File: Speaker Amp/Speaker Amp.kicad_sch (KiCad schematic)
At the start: 52 parts, among them J1 USB_C_Receptacle_USB2.0_16P, J2 Screw_Terminal_01x02, J3 Screw_Terminal_01x02, J4 Screw_Terminal_01x02, SW1 SW_Push, SW2 SW_Push, SW3 SW_Push, U1 LD1117S33TR_SOT223, U2 PCM2704CDBR, U3 TDA7297, U4 CH221K, Y1 12M

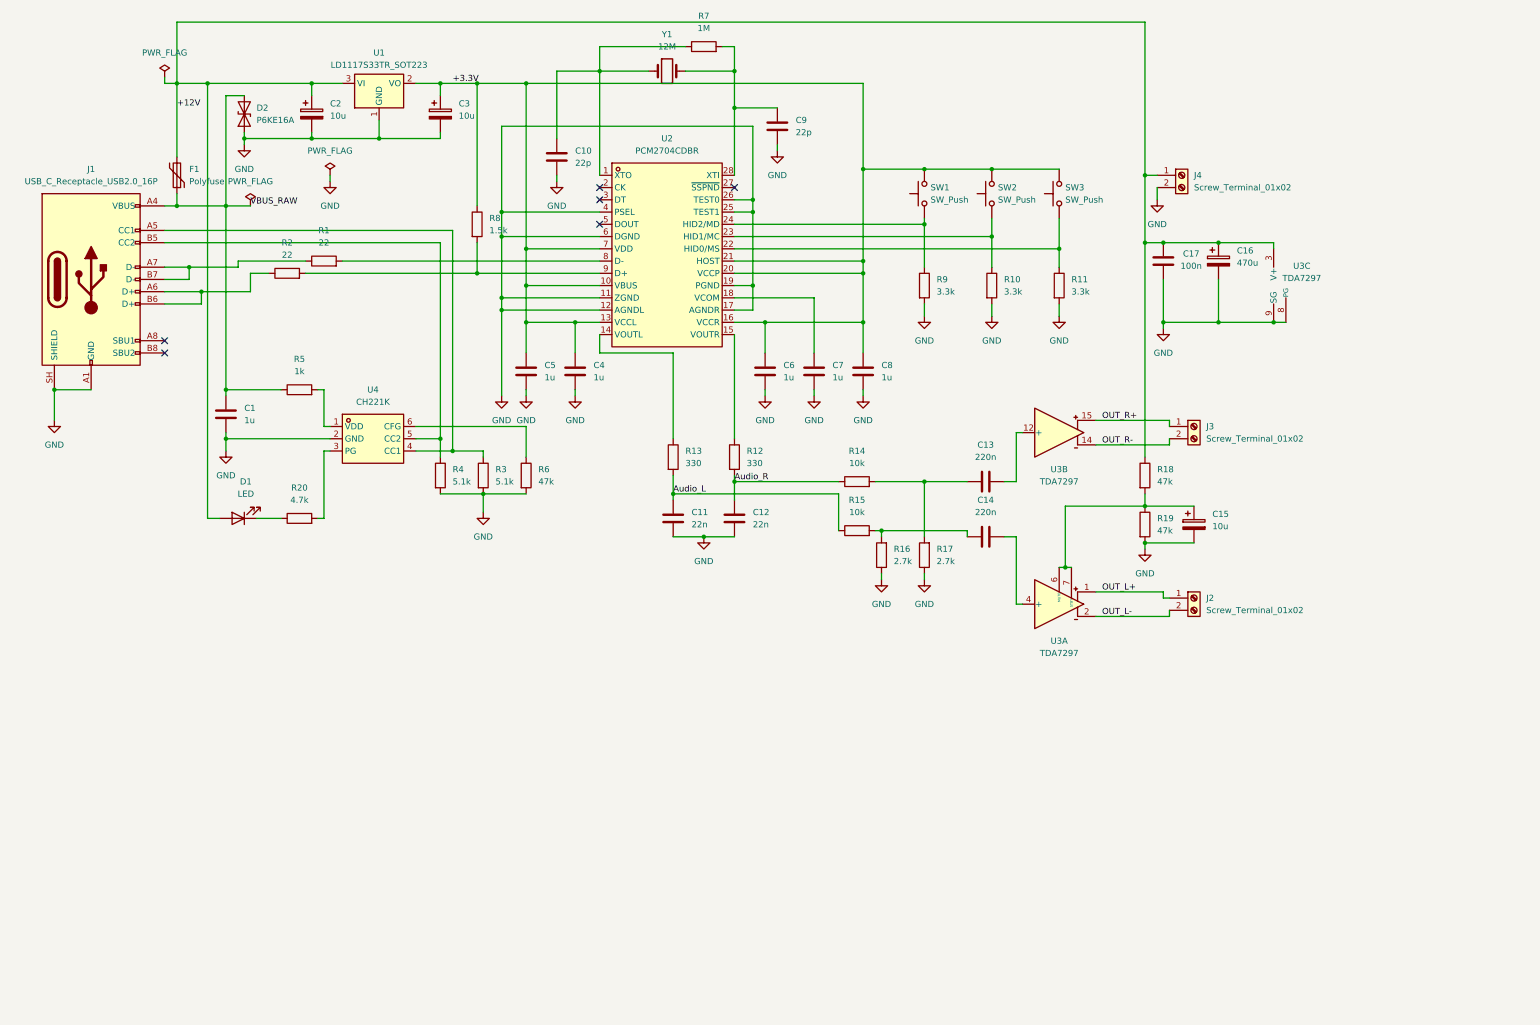
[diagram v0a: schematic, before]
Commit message: Speaker Amp: JLC-stockable parts - 3225 crystal, XUNPU TS-1005B SMD side buttons
Y1 swapped to 2-pin-mapped 3225 footprint (basic-part crystals); SW1-SW3
swapped to SMD side-press switches (LCSC C2856783, machine-assembled),
rotated to face the board edge with bracket anchors at the edge. 3.3V
button rail moved to a B.Cu pad-via rail; HID1/HID2 rerouted on B.Cu
around the USB differential pair. DRC: 0 errors, 0 unconnected, 0 parity.

Co-Authored-By: Claude Fable 5 <noreply@anthropic.com>
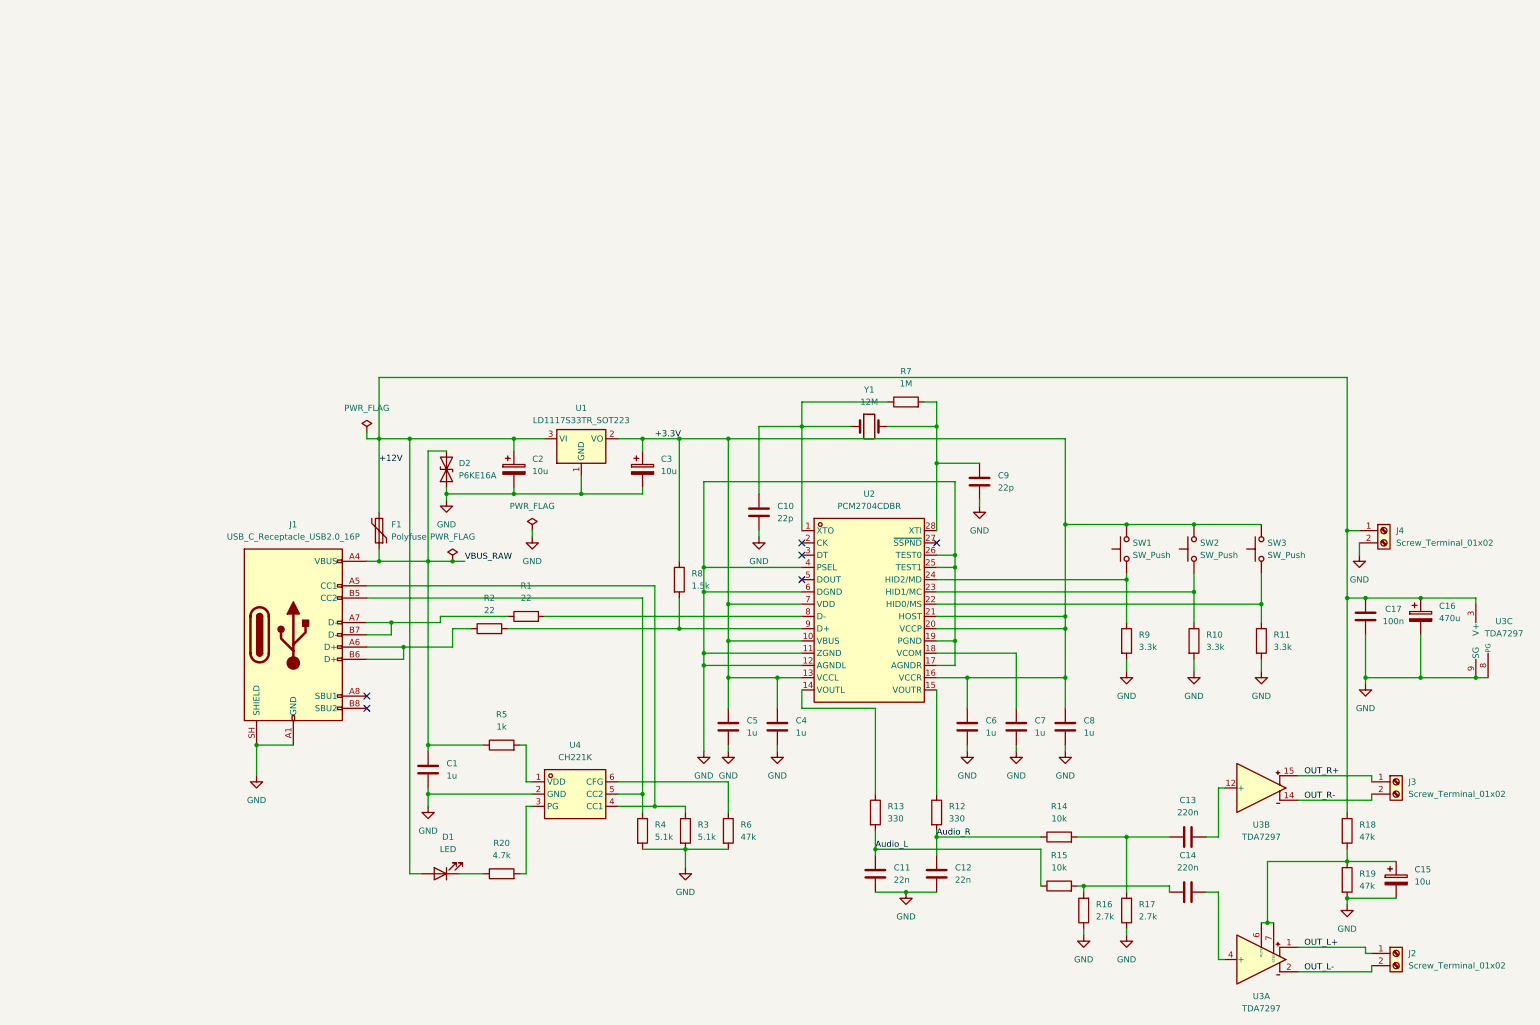
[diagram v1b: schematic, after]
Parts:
- SW1, SW2, SW3: footprint Button_Switch_THT:SW_Tactile_SPST_Angled_PTS645Vx58-2LFS -> SpeakerAmp:SW_TS-1005B_2PinMapped
- Y1: footprint Crystal:Crystal_SMD_5032-2Pin_5.0x3.2mm -> SpeakerAmp:Crystal_SMD_3225_2PinMapped
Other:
- moved on the sheet: C1, C10, C11, C12, C13, C14, C15, C16, C17, C2, C3, C4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

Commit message: Speaker Amp: swap 5.08mm Phoenix terminals to 3.5mm 4Ucon (Detkin stock)
In-place footprint swap for J2/J3/J4, pads recentered on the old blocks,
nets preserved, Phoenix PT-1,5 step model attached (no 4Ucon model ships).
Electrolytics already matched the user's THT caps. DRC unchanged: only the
accepted R6 starved-thermal.

Co-Authored-By: Claude Fable 5 <noreply@anthropic.com>
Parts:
- J2, J3, J4: footprint TerminalBlock_Phoenix:TerminalBlock_Phoenix_MKDS-1,5-2-5.08_1x02_P5.08mm_Horizontal -> TerminalBlock_4Ucon:TerminalBlock_4Ucon_1x02_P3.50mm_Horizontal
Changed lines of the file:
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@@
 			)
 		)
-		(property "Footprint" "TerminalBlock_Phoenix:TerminalBlock_Phoenix_MKDS-1,5-2-5.08_1x02_P5.08mm_Horizontal"
+		(property "Footprint" "TerminalBlock_4Ucon:TerminalBlock_4Ucon_1x02_P3.50mm_Horizontal"
 			(at 318.77 208.28 0)
 			(hide yes)
@@
 			)
 		)
-		(property "Footprint" "TerminalBlock_Phoenix:TerminalBlock_Phoenix_MKDS-1,5-2-5.08_1x02_P5.08mm_Horizontal"
+		(property "Footprint" "TerminalBlock_4Ucon:TerminalBlock_4Ucon_1x02_P3.50mm_Horizontal"
 			(at 316.23 120.65 0)
 			(hide yes)
@@
 			)
 		)
-		(property "Footprint" "TerminalBlock_Phoenix:TerminalBlock_Phoenix_MKDS-1,5-2-5.08_1x02_P5.08mm_Horizontal"
+		(property "Footprint" "TerminalBlock_4Ucon:TerminalBlock_4Ucon_1x02_P3.50mm_Horizontal"
 			(at 318.77 172.72 0)
 			(hide yes)

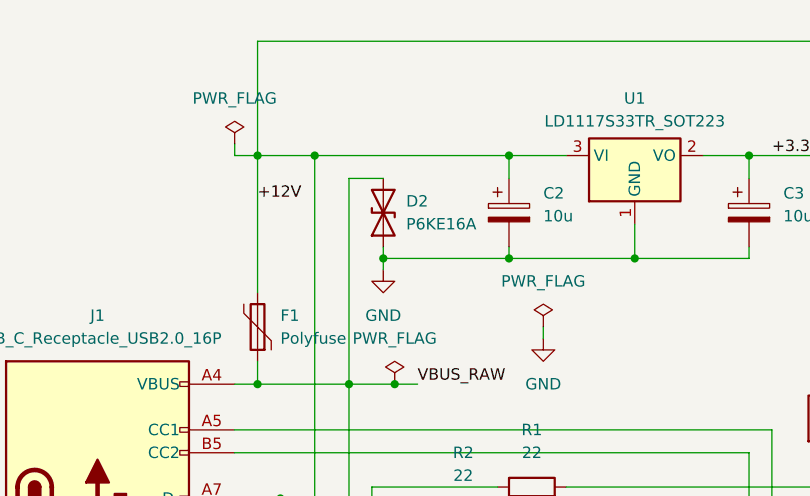
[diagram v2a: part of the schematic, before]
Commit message: Speaker Amp V4: JLC-mountable protection parts, THT indicator LED
- D2: P6KE16A DO-15 -> SMBJ15A SMB (JLC Preferred C19077569); schematic
  symbol rotated so the cathode pad lands on VBUS_RAW for assembly polarity
- F1: Bourns MF-RG300 radial -> SMD1812P300TF/16 3A/16V 1812 (C702820);
  C_1812 chip step model as stand-in (no 1812 fuse model ships)
- D1: APA1606 side LED -> LED_THT:LED_D5.0mm (Detkin stock, matches visualizer)
- User rework of the power-entry routing; one missing VBUS_RAW F/B via
  restored where the old D2 through-hole used to bridge layers
- DRC: 0 violations except accepted R6 starved-thermal, 0 unconnected
- V4 render set

Co-Authored-By: Claude Fable 5 <noreply@anthropic.com>
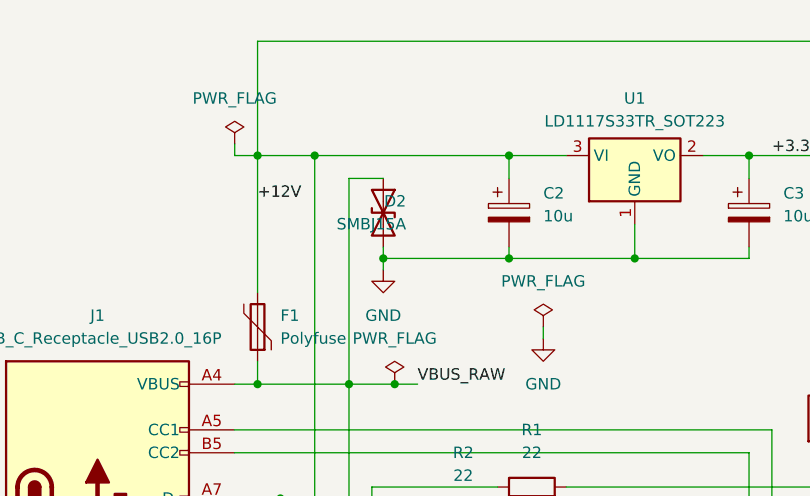
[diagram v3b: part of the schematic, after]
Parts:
- D1: footprint LED_SMD:LED_Kingbright_APA1606_1.6x0.6mm_Horizontal -> LED_THT:LED_D5.0mm
- D2: value P6KE16A -> SMBJ15A; footprint Diode_THT:D_DO-15_P10.16mm_Horizontal -> Diode_SMD:D_SMB
- F1: footprint Fuse:Fuse_Bourns_MF-RG300 -> Fuse:Fuse_1812_4532Metric
- U2: LCSC Part C2859784 -> C19077569
- U4: LCSC Part C5125736 -> C702820
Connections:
- net GND: now also D2.2 (A2); no longer D2.1 (A1)
- net VBUS_RAW: now also D2.1 (A1); no longer D2.2 (A2)
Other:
- moved on the sheet: D2
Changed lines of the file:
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@@
 			)
 		)
-		(property "LCSC Part" "C5125736"
+		(property "LCSC Part" "C702820"
 			(at 148.59 195.58 0)
 			(hide yes)
@@
 			)
 		)
-		(property "Footprint" "LED_SMD:LED_Kingbright_APA1606_1.6x0.6mm_Horizontal"
+		(property "Footprint" "LED_THT:LED_D5.0mm"
 			(at 120.65 191.77 0)
 			(hide yes)
@@
 	(symbol
 		(lib_id "Device:D_TVS")
-		(at 121.92 107.95 90)
+		(at 121.92 107.95 270)
 		(unit 1)
 		(body_style 1)
@@
 			)
 		)
-		(property "Value" "P6KE16A"
+		(property "Value" "SMBJ15A"
 			(at 124.46 109.2199 90)
 			(show_name no)
@@
 			)
 		)
-		(property "Footprint" "Diode_THT:D_DO-15_P10.16mm_Horizontal"
+		(property "Footprint" "Diode_SMD:D_SMB"
 			(at 121.92 107.95 0)
 			(hide yes)
@@
 			)
 		)
-		(property "LCSC Part" "C2859784"
+		(property "LCSC Part" "C19077569"
 			(at 209.55 171.45 0)
 			(hide yes)
@@
 			)
 		)
-		(property "Footprint" "Fuse:Fuse_Bourns_MF-RG300"
+		(property "Footprint" "Fuse:Fuse_1812_4532Metric"
 			(at 106.68 115.57 0)
 			(hide yes)

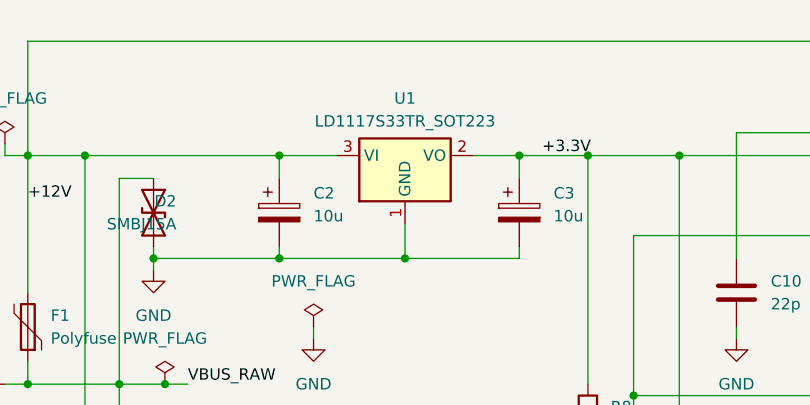
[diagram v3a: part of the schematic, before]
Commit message: Speaker Amp: Basic-catalog U1/Y1, fab package refresh
- U1: LD1117S33 -> AMS1117-3.3 (C6186, Basic, pin-compatible SOT-223)
- Y1: explicit LCSC C9002 (12MHz 3225, Basic) so the matcher stops
  whiffing on the custom 2-pin-remapped footprint name
- D2 C19077569 confirmed on JLC's Preferred list (no fee despite the
  Extended label in the matcher UI)
- Remaining fee-carrying Extended: F1, J1, SW1-3, U2, U4 (+U3 unless DNP)

Co-Authored-By: Claude Fable 5 <noreply@anthropic.com>
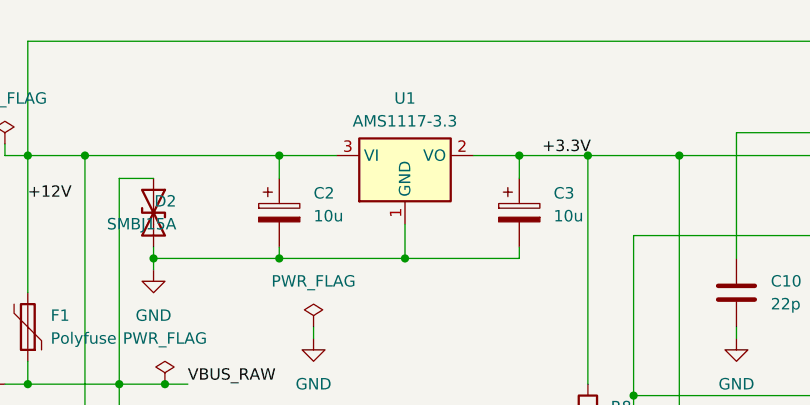
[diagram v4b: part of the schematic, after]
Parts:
- U1: value LD1117S33TR_SOT223 -> AMS1117-3.3; LCSC Part (none) -> C6186
- Y1: LCSC Part (none) -> C9002
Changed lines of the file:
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@@
 			)
 		)
-		(property "Value" "LD1117S33TR_SOT223"
+		(property "Value" "AMS1117-3.3"
 			(at 149.86 97.79 0)
 			(show_name no)
@@
 			)
 		)
+		(property "LCSC Part" "C6186"
+				(at 0 -20.32 0)
+				(show_name no)
+				(do_not_autoplace no)
+				(hide yes)
+				(effects
+					(font
+						(size 1.27 1.27)
+					)
+				)
+			)
 		(property "Footprint" "Package_TO_SOT_SMD:SOT-223-3_TabPin2"
 			(at 149.86 96.52 0)
@@
 			)
 		)
+		(property "LCSC Part" "C9002"
+				(at 0 -20.32 0)
+				(show_name no)
+				(do_not_autoplace no)
+				(hide yes)
+				(effects
+					(font
+						(size 1.27 1.27)
+					)
+				)
+			)
 		(property "Footprint" "SpeakerAmp:Crystal_SMD_3225_2PinMapped"
 			(at 209.55 99.06 0)
